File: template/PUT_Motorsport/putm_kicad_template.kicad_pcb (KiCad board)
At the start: 2 copper layers, 60 x 40 mm, 4 parts

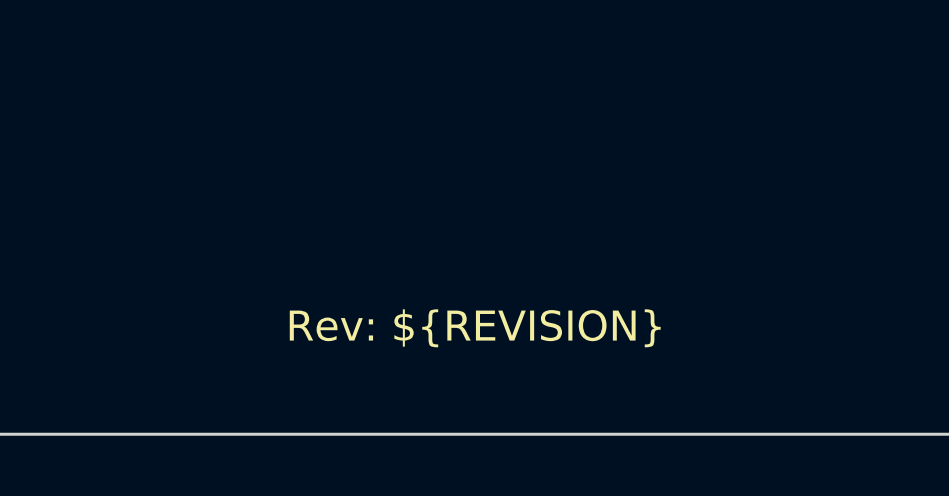
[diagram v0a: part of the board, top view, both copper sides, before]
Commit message: Adjust the minimum via annular width
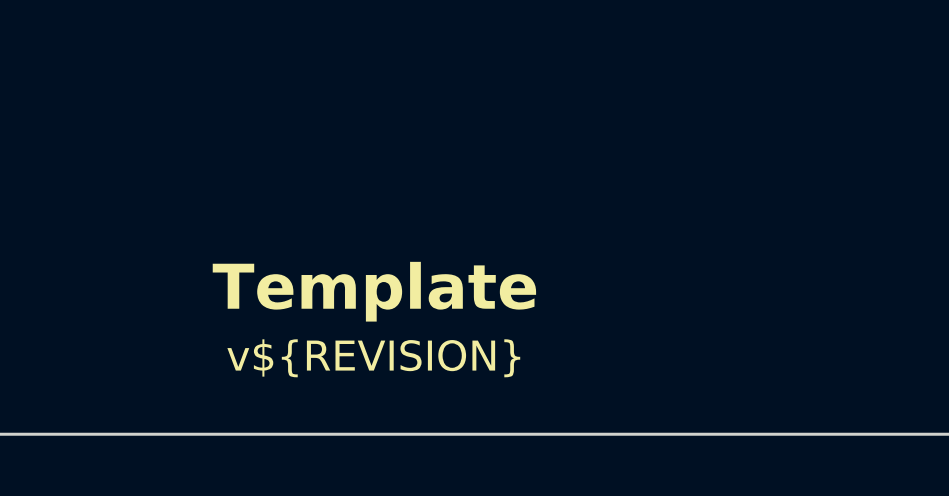
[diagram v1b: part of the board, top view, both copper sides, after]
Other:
- board text added: "Template"
- board text added: "v${REVISION}"
- board text removed: "Rev: ${REVISION}"
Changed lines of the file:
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@@
   (gr_arc (start 174 76) (mid 175.414214 76.585786) (end 176 78)
     (stroke (width 0.1) (type default)) (layer "Edge.Cuts"))
-  (gr_text "Rev: ${REVISION}" (at 143 113) (layer "F.SilkS")
-    (effects (font (size 1 1) (thickness 0.15)) (justify left bottom))
+  (gr_text "Template" (at 146 112) (layer "F.SilkS")
+    (effects (font (size 1.5 1.5) (thickness 0.3) bold) (justify bottom))
+  )
+  (gr_text "v${REVISION}" (at 146 114) (layer "F.SilkS")
+    (effects (font (size 1 1) (thickness 0.15)) (justify bottom))
   )
   (dimension (type aligned) (layer "Dwgs.User")
@@
     (style (thickness 0.15) (arrow_length 1.27) (text_position_mode 1) (extension_height 0.58642) (extension_offset 0.5) keep_text_aligned)
   )
+  (group "" (id 423d4aa3-e0ae-4d5e-8b84-ecca8a4a8613)
+    (members
+      5ba3910d-c4f2-472e-8687-e99a4b526b88
+      7aec6c76-b5f7-446f-9417-fb725641127b
+    )
+  )
 )
